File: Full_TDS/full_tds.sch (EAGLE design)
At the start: 69 parts, among them IC1 MCP1702, Q1 NFET, Q2 PFET, Q3 NFET, Q4 PFET, Q9 8MHz, U1 ATMEGA328P_PDIP, U2 FT232RLSSOP, U3 ADXL345PATRICK, U4 MPL3115A2LGA8, X2 USBSMD

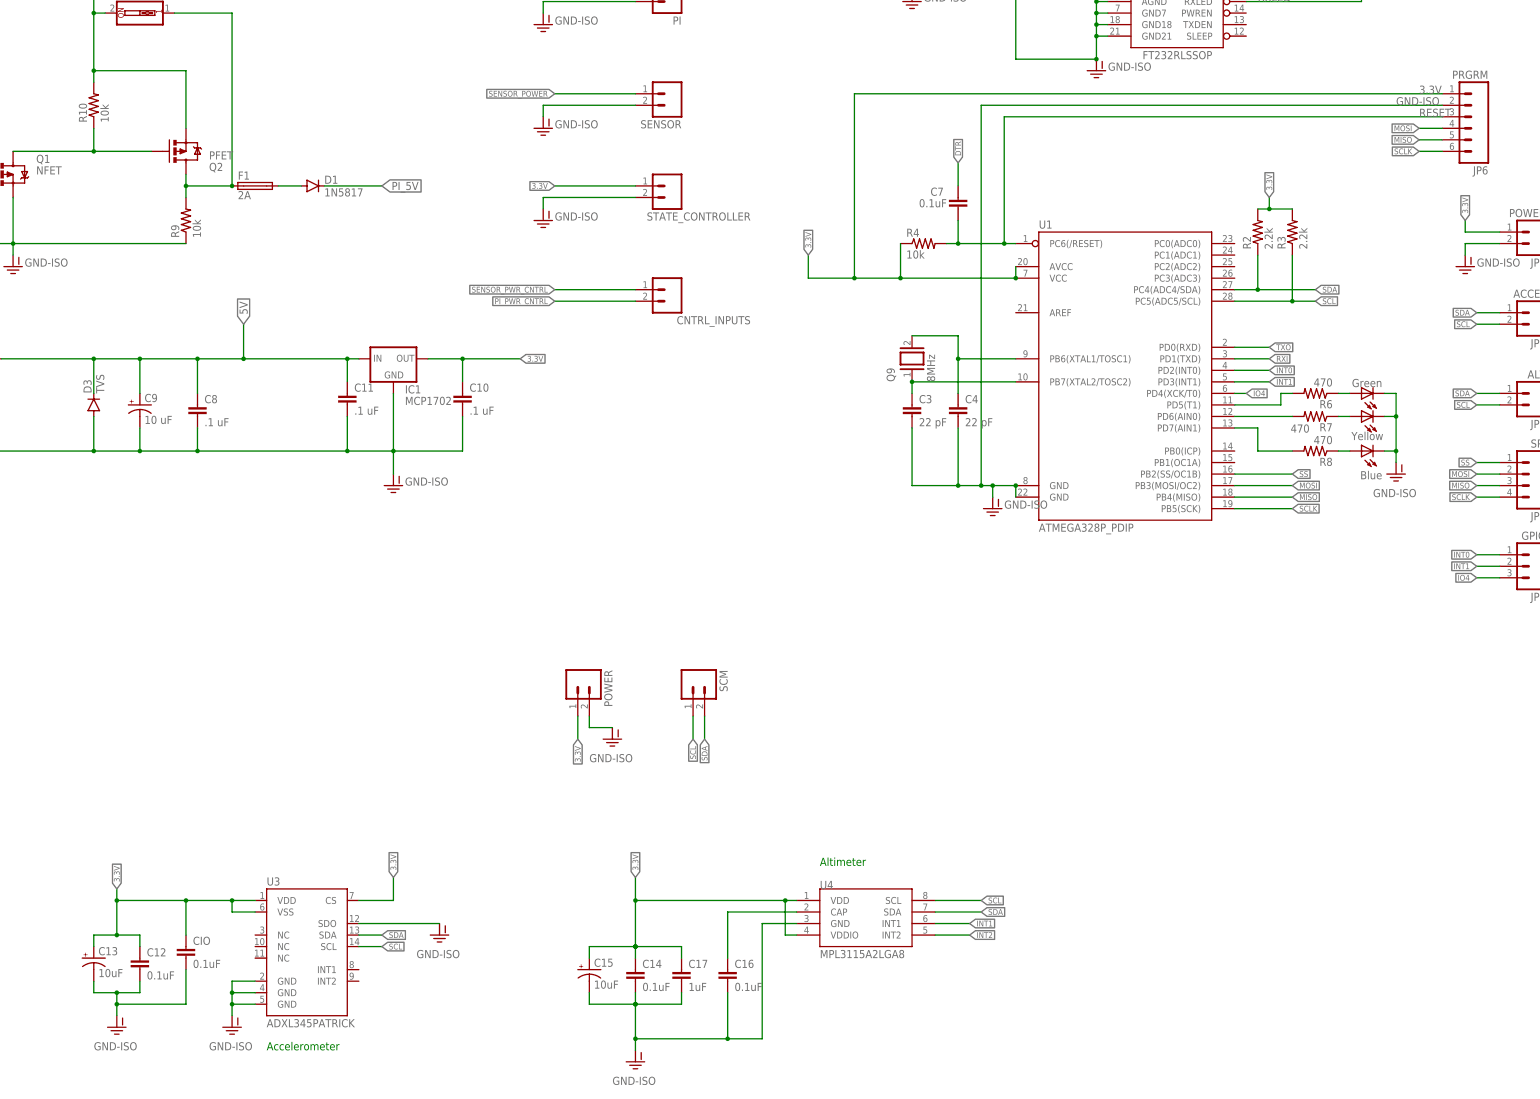
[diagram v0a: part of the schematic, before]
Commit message: Switched to QFP
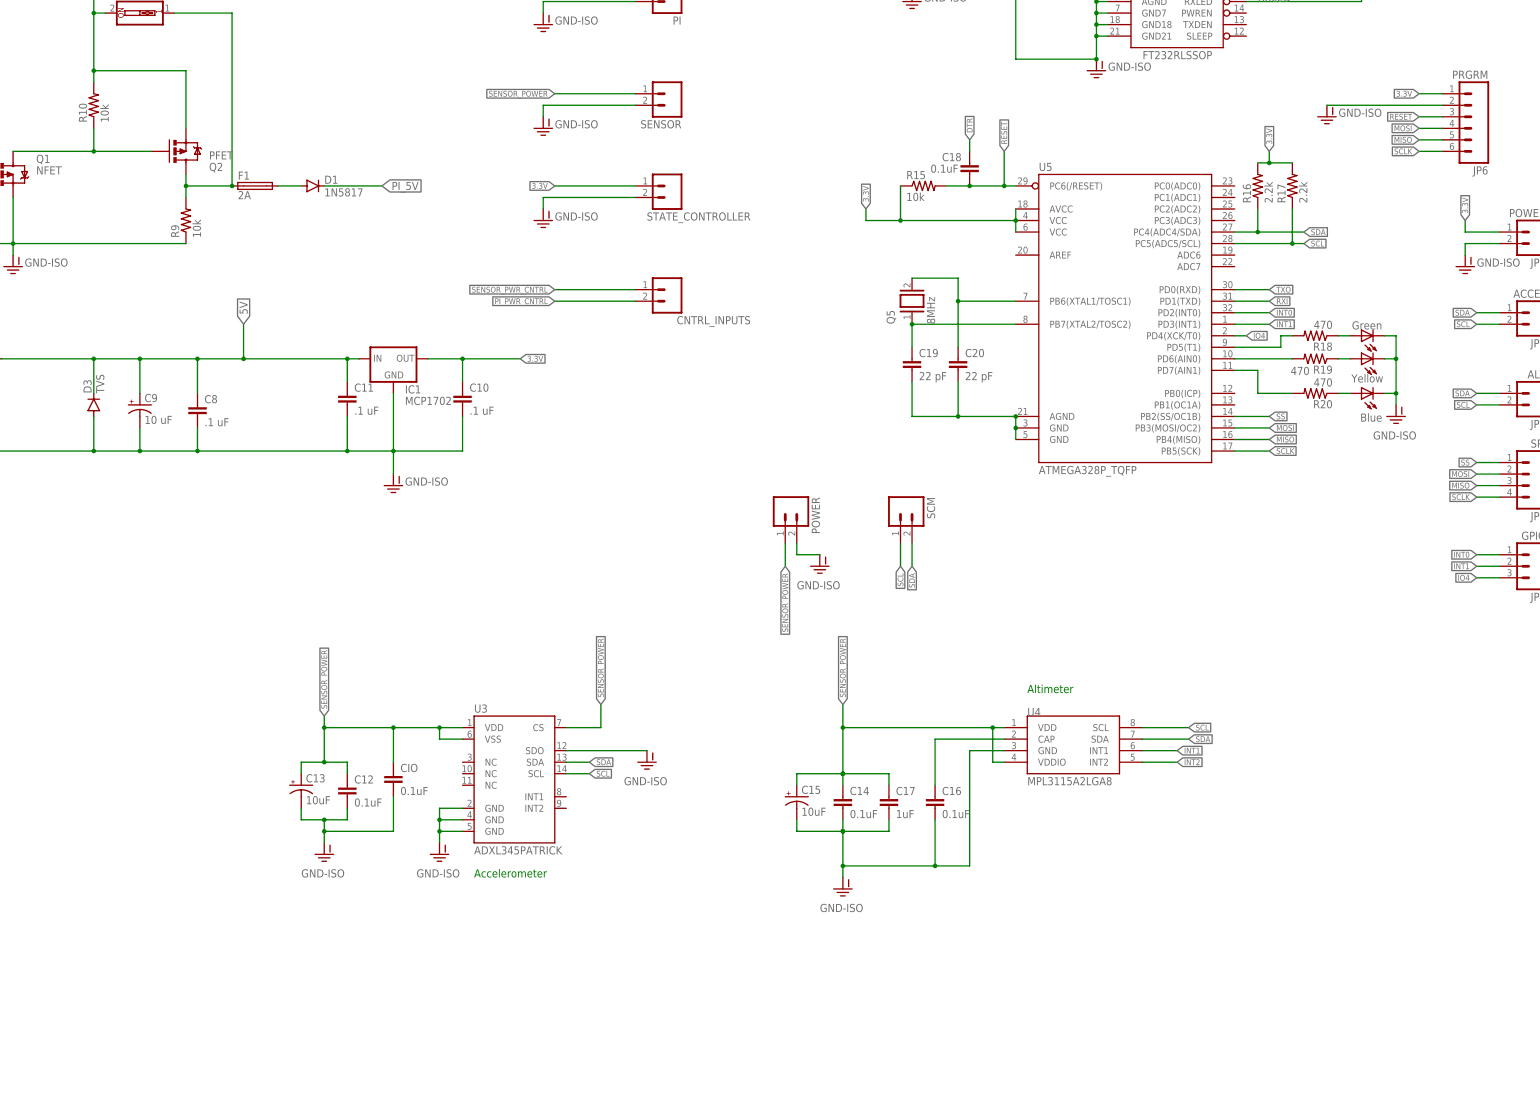
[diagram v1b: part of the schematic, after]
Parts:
- removed C3, C4: 22 pF, SparkFun-Capacitors:CAPPTH
- removed C7: 0.1uF, SparkFun-Capacitors:CAPPTH
- removed LED4: Yellow, adafruit:LED5MM
- removed LED5: Blue, adafruit:LED5MM
- removed Q9: 8MHz, special:XTAL/S
- removed R2, R3: 2.2k, SparkFun-Passives:RESISTOR1206
- removed R4: 10k, SparkFun-Passives:RESISTOR1206
- removed R7, R8: 470, SparkFun-Passives:RESISTOR1206
- removed U1: ATMEGA328P_PDIP, SparkFun-DigitalIC:ATMEGA328P_PDIP
- added C18: 0.1uF, SparkFun-Capacitors:CAPPTH
- added C19, C20: 22 pF, SparkFun-Capacitors:CAPPTH
- added LED6: Green, adafruit:LED5MM
- added LED7: Yellow, adafruit:LED5MM
- added Q5: 8MHz, special:XTAL/S
- added R15: 10k, SparkFun-Passives:RESISTOR1206
- added R16, R17: 2.2k, SparkFun-Passives:RESISTOR1206
- added R18, R19: 470, SparkFun-Passives:RESISTOR1206
- added U5: ATMEGA328P_TQFP, SparkFun-IC-Microcontroller:ATMEGA328P_TQFP
- LED8: value Green -> Blue
- renumbered LED3 to LED8, R6 to R20
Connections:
- removed net N$10: LED5.A, R8.1
- removed net N$11: C3.1, Q9.1, U1.PB7(XTAL2/TOSC2)
- removed net N$20: C4.1, Q9.2, U1.PB6(XTAL1/TOSC1)
- removed net N$5: R20.2, U1.PD5(T1)
- removed net N$6: R7.2, U1.PD6(AIN0)
- removed net N$7: R8.2, U1.PD7(AIN1)
- removed net N$9: LED4.A, R7.1
- new net N$18: C20.1, Q5.2, U5.PB6(XTAL1/TOSC1)
- new net N$19: C19.1, Q5.1, U5.PB7(XTAL2/TOSC2)
- new net N$21: R18.2, U5.PD5(T1)
- new net N$22: C19.2, C20.2, U5.AGND, U5.GND@3, U5.GND@5
- new net N$23: R19.2, U5.PD6(AIN0)
- new net N$24: R20.2, U5.PD7(AIN1)
- new net N$25: LED6.A, R18.1
- new net N$26: LED7.A, R19.1
- net 3.3V: now also R15.1, R16.2, R17.2, U5.AVCC, U5.VCC@4, U5.VCC@6; no longer C12.1, C13.+, C14.1, C15.+, C17.1, CIO.1, POWER.1, R2.2, R3.2, R4.1, U1.AVCC, U1.VCC, U3.CS, U3.VDD, U3.VSS, U4.VDD, U4.VDDIO
- net DTR: now also C18.1; no longer C7.1
- net GND-ISO: now also LED6.C, LED7.C; no longer C3.2, C4.2, LED4.C, LED5.C, U1.GND@1, U1.GND@2
- net INT0: now also U5.PD2(INT0); no longer U1.PD2(INT0)
- net INT1: now also U5.PD3(INT1); no longer U1.PD3(INT1)
- net IO4: now also U5.PD4(XCK/T0); no longer U1.PD4(XCK/T0)
- net MISO: now also U5.PB4(MISO); no longer U1.PB4(MISO)
- net MOSI: now also U5.PB3(MOSI/OC2); no longer U1.PB3(MOSI/OC2)
- net RESET: now also C18.2, R15.2, U5.PC6(/RESET); no longer C7.2, R4.2, U1.PC6(/RESET)
- net RXI: now also U5.PD1(TXD); no longer U1.PD1(TXD)
- net SCL: now also R17.1, U5.PC5(ADC5/SCL); no longer R3.1, U1.PC5(ADC5/SCL)
- net SCLK: now also U5.PB5(SCK); no longer U1.PB5(SCK)
- net SDA: now also R16.1, U5.PC4(ADC4/SDA); no longer R2.1, U1.PC4(ADC4/SDA)
- net SENSOR_POWER: now also C12.1, C13.+, C14.1, C15.+, C17.1, CIO.1, POWER.1, U3.CS, U3.VDD, U3.VSS, U4.VDD, U4.VDDIO
- net SS: now also U5.PB2(SS/OC1B); no longer U1.PB2(SS/OC1B)
- net TXO: now also U5.PD0(RXD); no longer U1.PD0(RXD)
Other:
- moved on the sheet: C12, C13, C14, C15, C16, C17, CIO, POWER, SCM, U3, U4

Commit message: Schem touch up
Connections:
- net PI_PWR_CNTRL: now also U5.PB1(OC1A)
- net SENSOR_PWR_CNTRL: now also U5.PB0(ICP)
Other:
- moved on the sheet: C11, C8, C9, D3, F3, JP1, JP2, JP3, JP4, JP5, JP6, JP7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

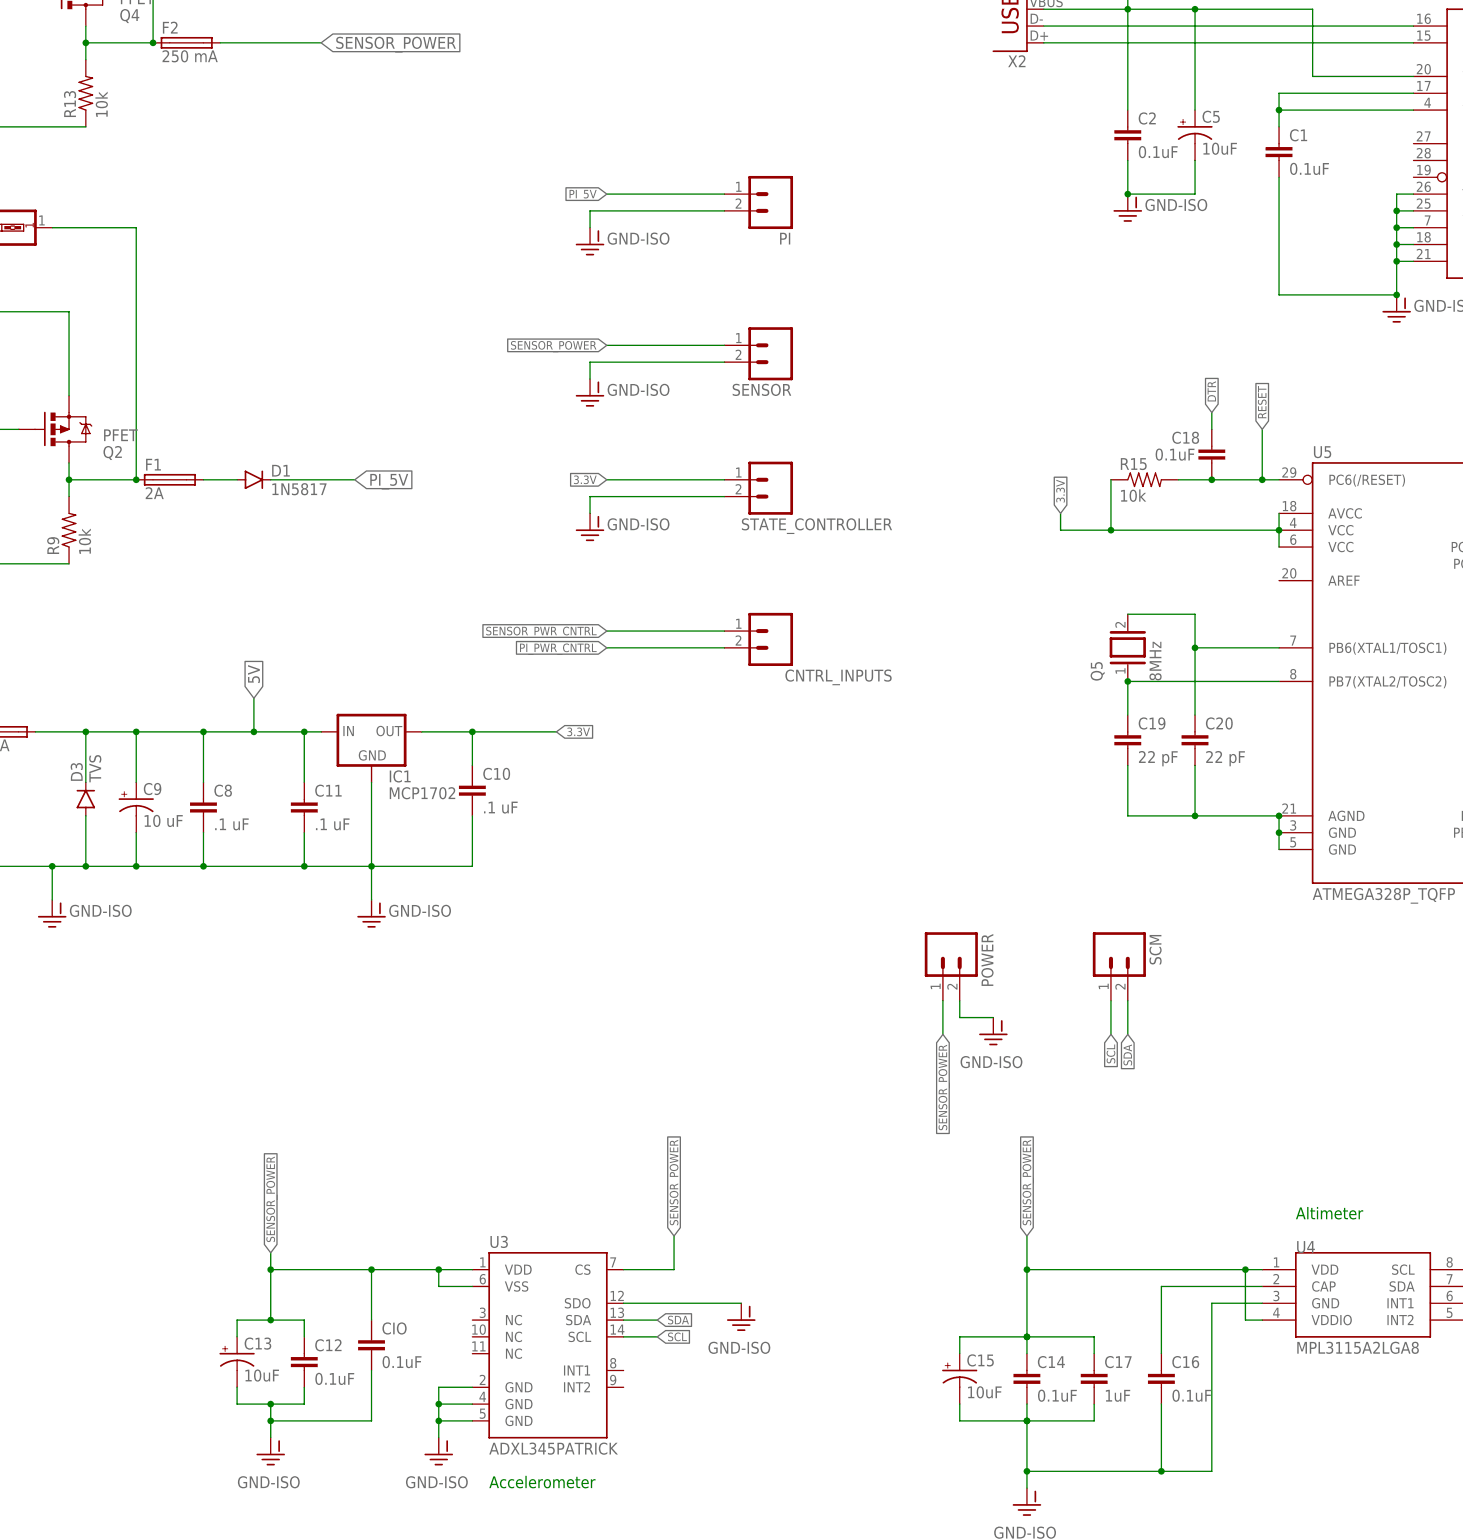
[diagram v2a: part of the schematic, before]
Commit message: Replaced capacitors with 1206
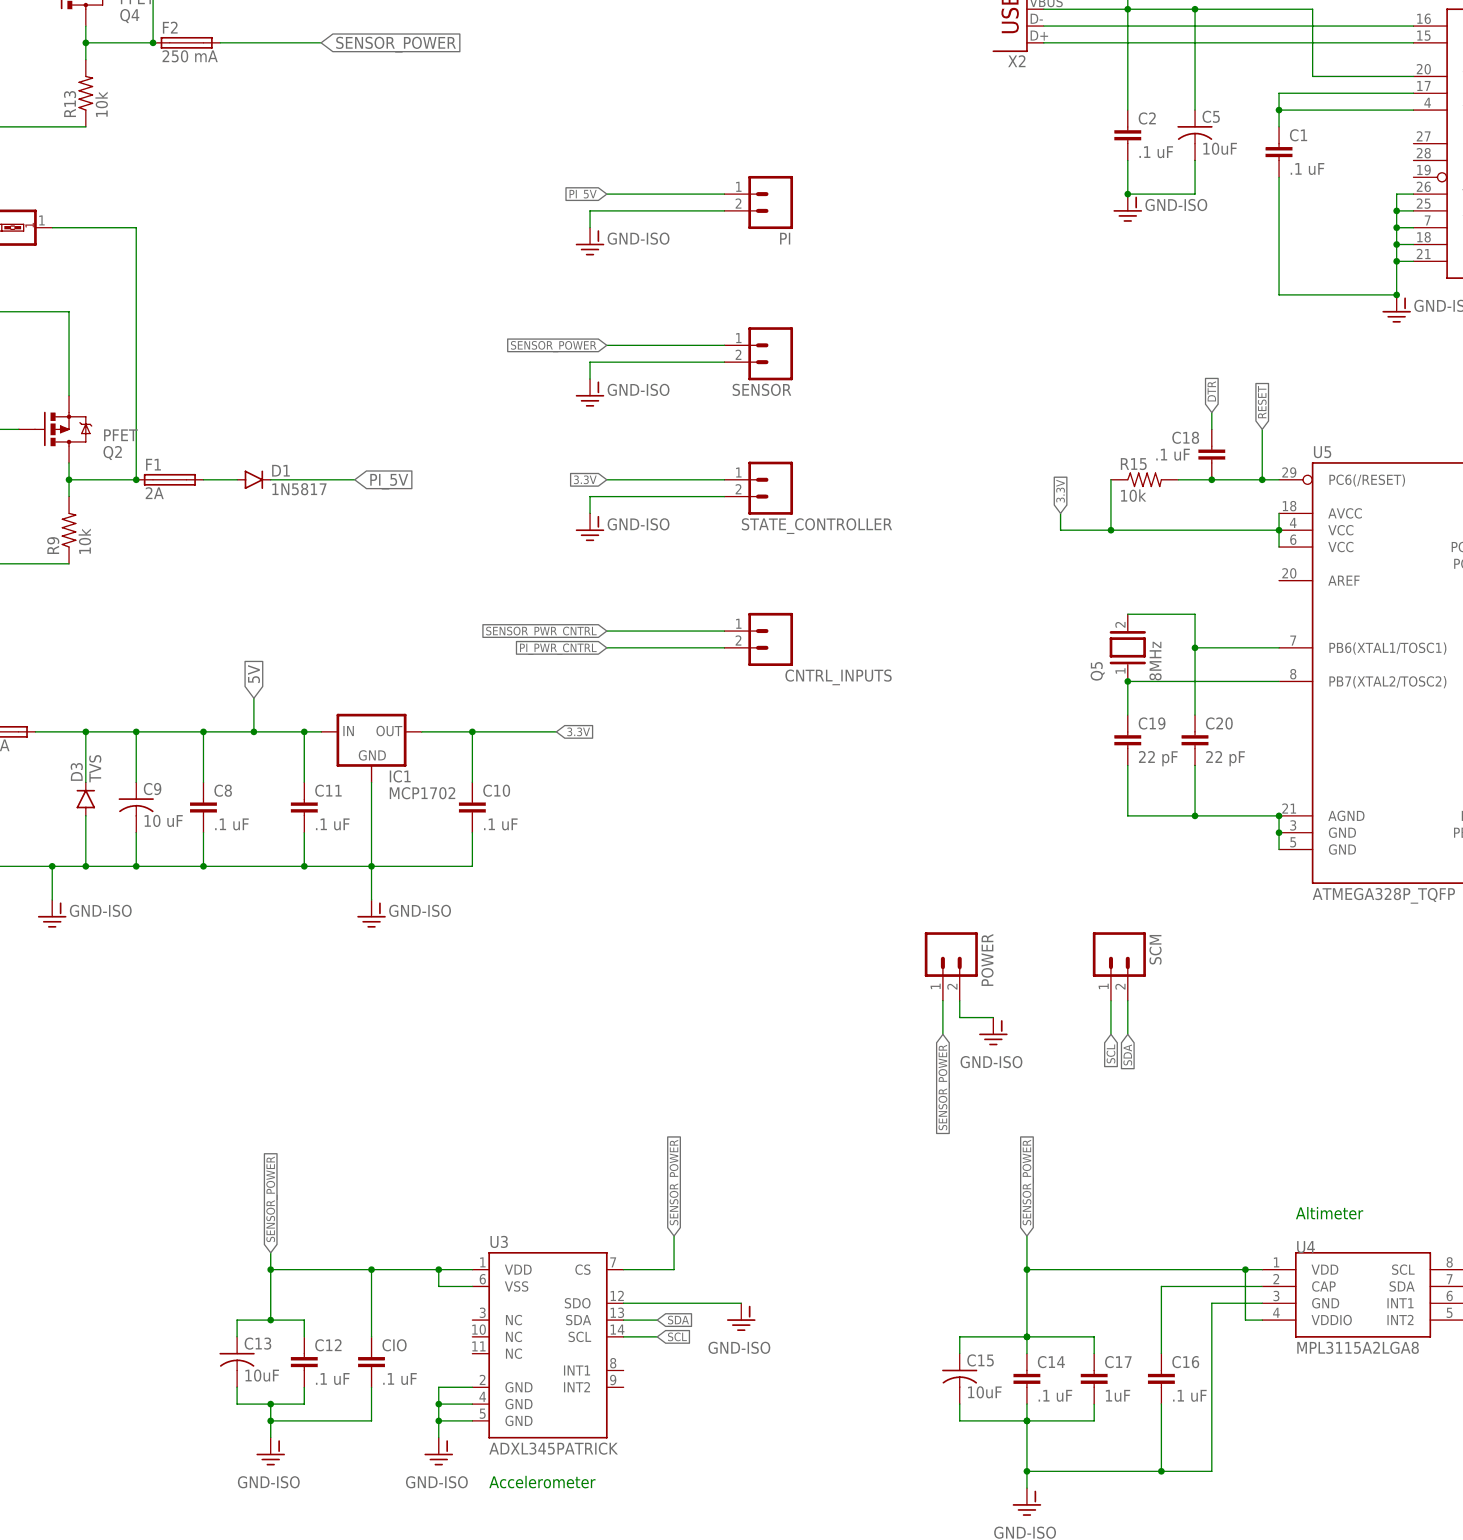
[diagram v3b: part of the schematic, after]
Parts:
- C1, C18, C2: value 0.1uF -> .1 uF; device SparkFun-Capacitors:CAPPTH -> SparkFun-Capacitors:1.0UF-1206-50V-10%
- C10, C11, C19, C20, C6: device SparkFun-Capacitors:CAPPTH -> SparkFun-Capacitors:1.0UF-1206-50V-10%
- C12, C14, CIO: value 0.1uF -> .1 uF; device SparkFun-Passives:CAPPTH -> SparkFun-Capacitors:1.0UF-1206-50V-10%
- C13, C15, C5, C9: device SparkFun-Passives:CAP_POLPTH2 -> adafruit:C-USC1206
- C16: value 0.1uF -> .1 uF
- C8: device SparkFun-Passives:CAPPTH -> SparkFun-Capacitors:1.0UF-1206-50V-10%
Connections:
- net 5V: now also C9.1; no longer C9.+
- net GND-ISO: now also C13.2, C15.2, C5.2, C9.2; no longer C13.-, C15.-, C5.-, C9.-
- net SENSOR_POWER: now also C13.1, C15.1; no longer C13.+, C15.+
- net VBUS: now also C5.1; no longer C5.+
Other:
- moved on the sheet: C10, CIO

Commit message: Replaced transistors with SMD part
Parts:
- removed Q1, Q3: NFET, User-Submitted:MOSFET-PCHANNELFQP27P06
- removed Q2, Q4: PFET, User-Submitted:MOSFET-PCHANNELFQP27P06
- removed X2: USBSMD, SparkFun-Connectors:USBSMD
- added JP8: USB-MICROB, SparkFun-Connectors:USB-MICROB
- added JP9: I2C, SparkFun-Connectors:M02PTH
- added U$1, U$2: DMC3021LSD-13, custom:DMC3021LSD-13
- C1, C10, C11, C12, C14, C18, C2, C8, CIO: value .1 uF -> 0.1 uF
- C16: value .1 uF -> 0.1 uF; device SparkFun-Passives:CAPPTH -> SparkFun-Capacitors:1.0UF-1206-50V-10%
- C17: value 1uF -> 1.0uF; device SparkFun-Passives:CAPPTH -> SparkFun-Capacitors:1.0UF-1206-50V-10%
- LED1, LED2, LED6, LED7, LED8: device adafruit:LED5MM -> adafruit:LEDCHIPLED_1206
- SW1: value (none) -> MAIN
- SW2: value (none) -> PI
- SW3: value (none) -> SENSOR
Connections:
- removed net INT2: U4.INT2
- removed net N$12: F1.1, Q2.D, R9.2, SW2.1
- removed net N$14: Q3.D, Q4.G, R14.1
- removed net N$15: F2.1, Q4.D, R13.2, SW3.1
- new net ACCEL_INT1: JP4.1, U3.INT1
- new net ACCEL_INT2: JP4.2, U3.INT2
- new net ALT_INT1: JP5.1, U4.INT1
- new net ALT_INT2: JP5.2, U4.INT2
- new net N$5: R14.1, U$1.D2(N), U$1.D2.(N), U$1.G1(P)
- new net N$6: F2.1, R13.2, SW3.1, U$1.D1(P), U$1.D1.(P)
- new net N$7: R10.1, U$2.D2(N), U$2.D2.(N), U$2.G1(P)
- net 3.3V: now also U$1.S1(P); no longer Q4.S
- net 5V: now also U$2.S1(P); no longer Q2.S
- net GND-ISO: now also JP8.GND, U$1.S2(N), U$2.S2(N); no longer Q1.S, Q3.S, X2.GND
- net INT1: no longer U4.INT1
- net N$3: now also F1.1, R9.2, SW2.1, U$2.D1(P), U$2.D1.(P); no longer Q1.D, Q2.G, R10.1
- net PI_PWR_CNTRL: now also U$2.G2(N); no longer Q1.G
- net SCL: now also JP9.2; no longer JP4.2, JP5.2
- net SDA: now also JP9.1; no longer JP4.1, JP5.1
- net SENSOR_PWR_CNTRL: now also U$1.G2(N); no longer Q3.G
- net USB_D+: now also JP8.D+; no longer X2.D+
- net USB_D-: now also JP8.D-; no longer X2.D-
- net VBUS: now also JP8.VBUS; no longer X2.VBUS
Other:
- moved on the sheet: C2, C5, C6, D1, F1, F2, JP7, R10, R11, R12, R13, R9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
